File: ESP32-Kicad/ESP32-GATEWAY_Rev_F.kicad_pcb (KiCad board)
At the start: 2 copper layers, 50.8 x 62.2 mm, 66 parts, among them J1 Conn_01x07_Male, T1 DTC114YKA, U1 ACPL-217-56AE, U2 TLV62569DBVT(SOT23-5), U3 ESP32-WROOM-32D-4MB, U4 LAN8710A-EZC(QFN32), U5 ACPL-217-56AE

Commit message: Placa de kicad actualizada
Se agregaron los optoacopladores en los sensores de puerta, y se movieron los logos en la silkscreen de Ericnet y JLCPCB para la capa de atrás.
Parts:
- added G2: LOGO JLCPCB, Logos personales:jlcpcb_logo, B.Cu at (108.7, 114.6)
- added G3: LOGO ERICNET, Logos personales:ericnet_logo, B.Cu at (82.9, 114.8)
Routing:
- net GND: vias 173 -> 172

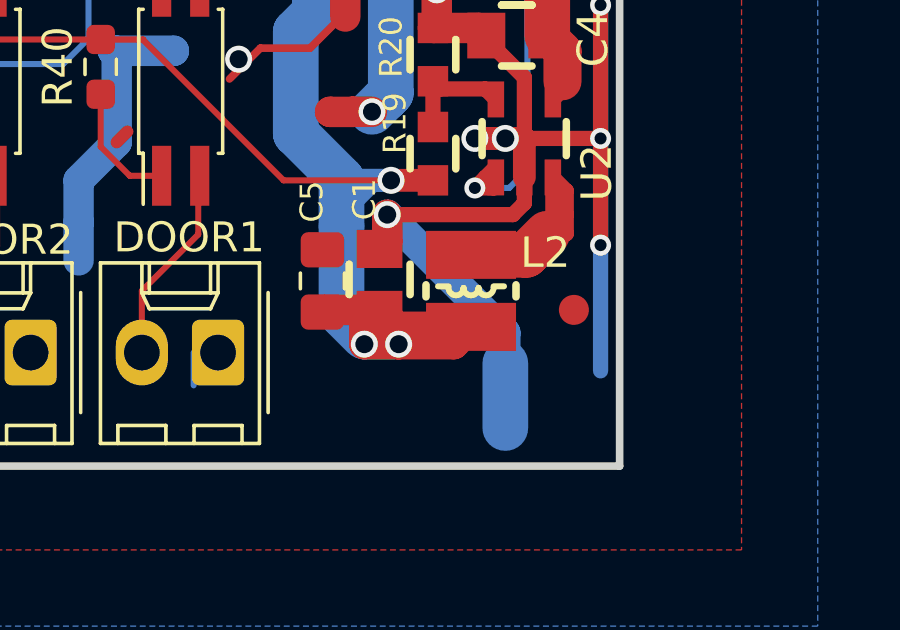
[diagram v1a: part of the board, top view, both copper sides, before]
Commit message: Proyecto en kicad actualizado
Se modificó el footprint del Inductor de la fuente
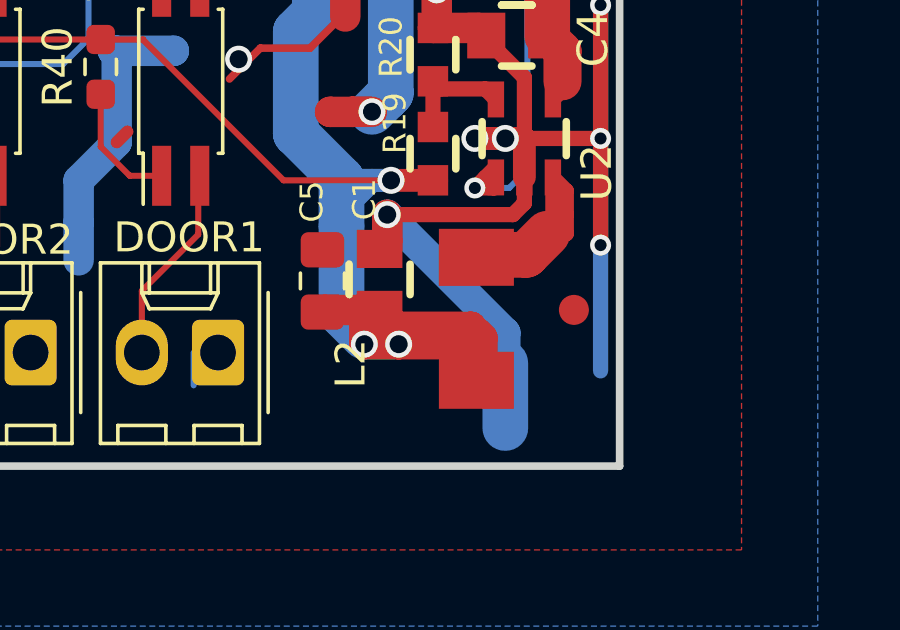
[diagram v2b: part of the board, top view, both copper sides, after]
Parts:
- L2: value 2.2uH/1.5A/DCR=35mR/20%/3.00x3.00x1.50mm/CD32(NR3015T2R2M) -> 2.2uH/9A/DCR=35mR/20%/3.00x3.00x1.50mm/CD32(NR3015T2R2M); footprint OLIMEX_RLC-FP:CD32 -> footprints_personales:SMD_0530
- moved L2 1.13 mm to (115.6, 122.3)
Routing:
- net +3V3: track 195.6 -> 197.8 mm

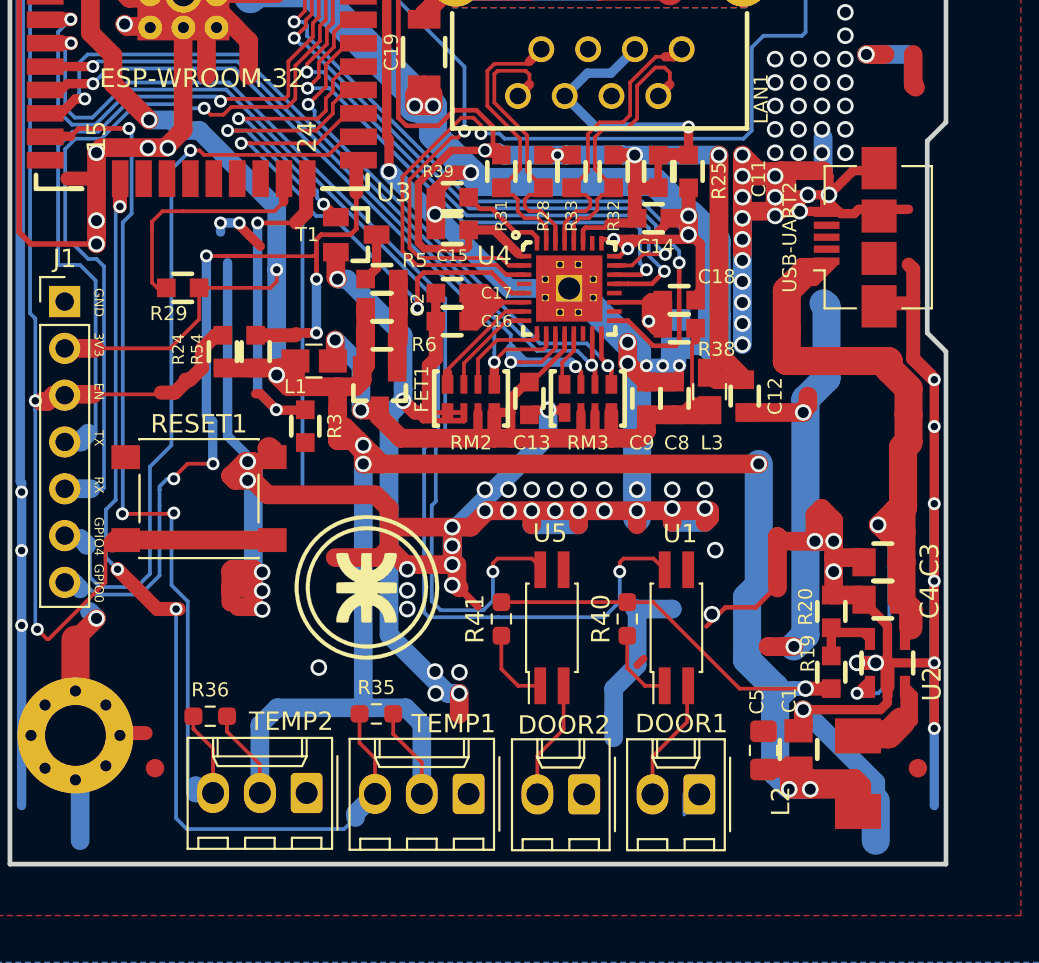
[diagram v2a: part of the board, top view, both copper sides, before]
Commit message: Se agregaron 2 sensores de puerta y se sacó uno de temperatura
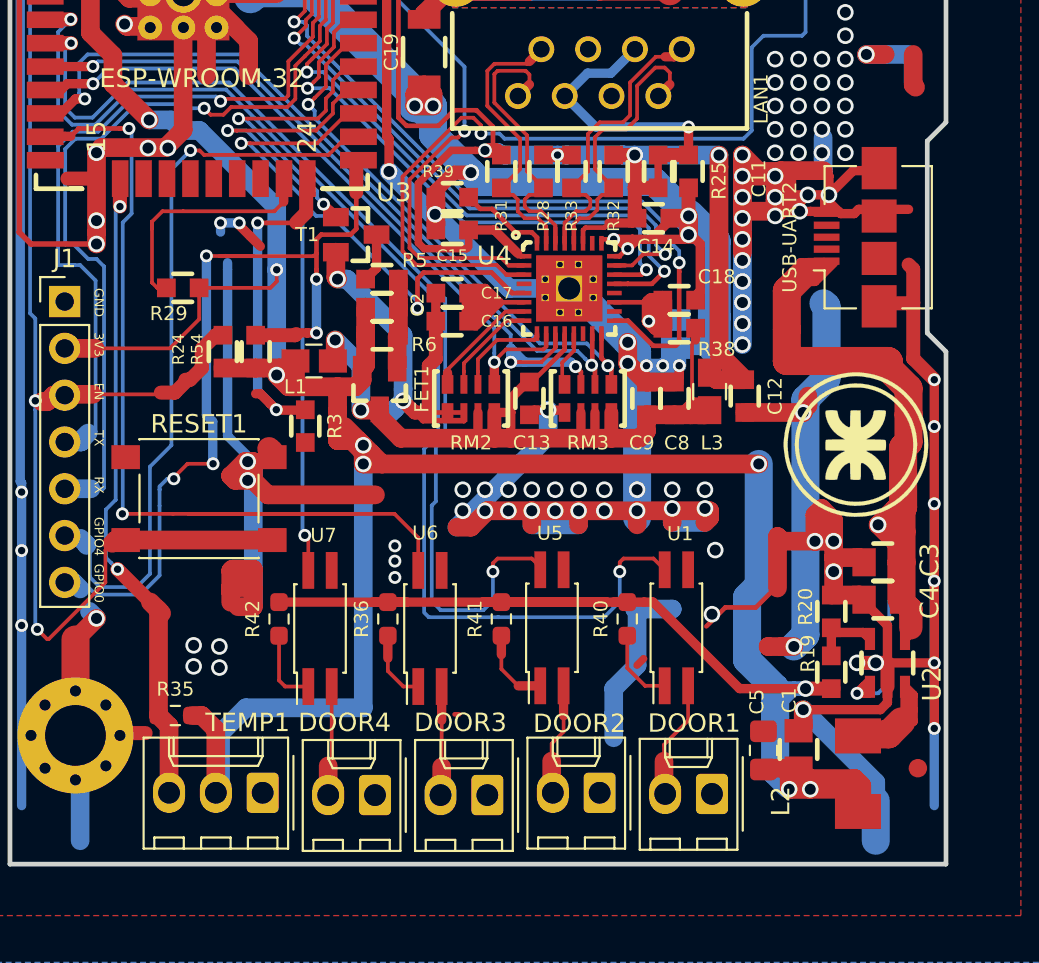
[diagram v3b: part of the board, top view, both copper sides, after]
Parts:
- removed FID1: Fiducial, OLIMEX_Other-FP:Fiducial1x3
- removed G1: Logo UTN, Logos personales:utn_logo
- removed TEMP2: Conn_01x03, Connector_Molex:Molex_KK-254_AE-6410-03A_1x03_P2.54mm_Vertical
- added DOOR3: Conn_01x02, Connector_Molex:Molex_KK-254_AE-6410-02A_1x02_P2.54mm_Vertical, F.Cu at (95.5, 125.5)
- added DOOR4: Conn_01x02, Connector_Molex:Molex_KK-254_AE-6410-02A_1x02_P2.54mm_Vertical, F.Cu at (89.4, 125.5)
- added G***: LOGO, Logos personales:utn_logo, F.Cu at (115.4, 106.6)
- added R42: 440/R0603, Resistor_SMD:R_0603_1608Metric_Pad0.98x0.95mm_HandSolder, F.Cu at (84.2, 116.0)
- added U6: ACPL-217-56AE, Package_SO:SO-4_4.4x2.3mm_P1.27mm, F.Cu at (92.4, 116.5)
- added U7: ACPL-217-56AE, Package_SO:SO-4_4.4x2.3mm_P1.27mm, F.Cu at (86.4, 116.5)
- R36: value 4.7K/R0603 -> 440/R0603
- moved TEMP1 11.2 mm to (83.3, 125.4)
- moved R36 11.0 mm to (90.1, 116.0), turned to 90 degrees
- moved R35 10.9 mm to (78.6, 121.2)
- moved DOOR2 0.84 mm to (101.6, 125.4)
- moved DOOR1 0.69 mm to (107.7, 125.5)
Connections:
- R36 pad 1: /GPIO14\TEMP2 -> Net-(R36-Pad1)
- U3 pad 13: /GPIO14\TEMP2 -> /GPIO14\DOOR3
- U3 pad 27: /GPIO16 -> /GPIO16\DOOR4
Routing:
- net /GPIO14\DOOR3: track 0.00 -> 54.0 mm, vias 0 -> 2
- net /GPIO14\TEMP2: track 51.1 -> 0.00 mm, vias 3 -> 0
- net GND: track 713.7 -> 672.1 mm, vias 172 -> 166
- net +3V3: track 197.8 -> 232.8 mm
- net /GPIO16\DOOR4: track 0.00 -> 32.1 mm, vias 0 -> 2
- net /GPIO16: track 27.8 -> 0.00 mm, vias 1 -> 0
- net /GPIO13\TEMP1: track 55.6 -> 35.9 mm, vias 3 -> 2
- net Net-(DOOR4-Pad2): track 0.00 -> 5.97 mm
- net Net-(DOOR3-Pad2): track 0.00 -> 5.92 mm
- net Net-(R36-Pad1): track 0.00 -> 4.69 mm
- net Net-(R42-Pad1): track 0.00 -> 3.92 mm
- net Net-(DOOR1-Pad2): track 6.69 -> 8.28 mm
- net Net-(DOOR2-Pad2): track 6.48 -> 7.81 mm

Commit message: Gerbers + ESP32 https server
Se agregaron gerbers y cambios finales de la placa. Se agrego un servidor https al codigo para el esp32
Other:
- board text added: "SNMP Hub Casas Daiana Pregelj Jose Riveros Rubén Vieiro Alexis"
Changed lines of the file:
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@@
   (general
     (thickness 1.6)
-    (drawings 19)
+    (drawings 20)
     (tracks 1715)
     (zones 0)
@@
   )
   (layers
-    (0 F.Cu mixed)
+    (0 F.Cu mixed hide)
     (31 B.Cu mixed)
     (32 B.Adhes user hide)
@@
     (35 F.Paste user hide)
     (36 B.SilkS user)
-    (37 F.SilkS user)
+    (37 F.SilkS user hide)
     (38 B.Mask user hide)
     (39 F.Mask user hide)
@@
     (42 Eco1.User user hide)
     (43 Eco2.User user hide)
-    (44 Edge.Cuts user hide)
+    (44 Edge.Cuts user)
     (45 Margin user hide)
     (46 B.CrtYd user hide)
@@
     (visible_elements 7FFDFF7F)
     (pcbplotparams
-      (layerselection 0x010fc_ffffffff)
+      (layerselection 0x3ffff_ffffffff)
       (usegerberextensions false)
       (usegerberattributes false)
@@
       (drillshape 0)
       (scaleselection 1)
-      (outputdirectory "../../../../Desktop/"))
+      (outputdirectory "Gerbers Propios/"))
   )
   (net 0 "")
@@
     (pad 2 thru_hole oval (at 2.54 0 180) (size 1.74 2.19) (drill 1.19) (layers *.Cu *.Mask)
       (net 74 "Net-(DOOR4-Pad2)"))
-    (pad 1 thru_hole roundrect (at 0 0 180) (size 1.74 2.19) (drill 1.19) (layers *.Cu *.Mask) (roundrect_rratio 0.143678)
+    (pad 1 thru_hole roundrect (at 0 0 180) (size 1.74 2.19) (drill 1.19) (layers *.Cu *.Mask) (roundrect_rratio 0.1436775862068966)
       (net 2 GND))
     (model ${KISYS3DMOD}/Connector_Molex.3dshapes/Molex_KK-254_AE-6410-02A_1x02_P2.54mm_Vertical.wrl
@@
     (pad 2 thru_hole oval (at 2.54 0 180) (size 1.74 2.19) (drill 1.19) (layers *.Cu *.Mask)
       (net 72 "Net-(DOOR3-Pad2)"))
-    (pad 1 thru_hole roundrect (at 0 0 180) (size 1.74 2.19) (drill 1.19) (layers *.Cu *.Mask) (roundrect_rratio 0.143678)
+    (pad 1 thru_hole roundrect (at 0 0 180) (size 1.74 2.19) (drill 1.19) (layers *.Cu *.Mask) (roundrect_rratio 0.1436775862068966)
       (net 2 GND))
     (model ${KISYS3DMOD}/Connector_Molex.3dshapes/Molex_KK-254_AE-6410-02A_1x02_P2.54mm_Vertical.wrl
@@
       (effects (font (size 0.5 0.5) (thickness 0.08)))
     )
-    (pad 2 smd roundrect (at 1.0375 0 90) (size 1.175 1.45) (layers F.Cu F.Paste F.Mask) (roundrect_rratio 0.212766)
+    (pad 2 smd roundrect (at 1.0375 0 90) (size 1.175 1.45) (layers F.Cu F.Paste F.Mask) (roundrect_rratio 0.2127659574468085)
       (net 2 GND))
-    (pad 1 smd roundrect (at -1.0375 0 90) (size 1.175 1.45) (layers F.Cu F.Paste F.Mask) (roundrect_rratio 0.212766)
+    (pad 1 smd roundrect (at -1.0375 0 90) (size 1.175 1.45) (layers F.Cu F.Paste F.Mask) (roundrect_rratio 0.2127659574468085)
       (net 3 +3V3))
     (model ${KISYS3DMOD}/Capacitor_SMD.3dshapes/C_0805_2012Metric.wrl
@@
     (pad 2 thru_hole oval (at 2.54 0 180) (size 1.74 2.19) (drill 1.19) (layers *.Cu *.Mask)
       (net 3 +3V3))
-    (pad 1 thru_hole roundrect (at 0 0 180) (size 1.74 2.19) (drill 1.19) (layers *.Cu *.Mask) (roundrect_rratio 0.143678)
+    (pad 1 thru_hole roundrect (at 0 0 180) (size 1.74 2.19) (drill 1.19) (layers *.Cu *.Mask) (roundrect_rratio 0.1436775862068966)
       (net 2 GND))
     (model ${KISYS3DMOD}/Connector_Molex.3dshapes/Molex_KK-254_AE-6410-03A_1x03_P2.54mm_Vertical.wrl
@@
     (pad 2 thru_hole oval (at 2.54 0 180) (size 1.74 2.19) (drill 1.19) (layers *.Cu *.Mask)
       (net 69 "Net-(DOOR2-Pad2)"))
-    (pad 1 thru_hole roundrect (at 0 0 180) (size 1.74 2.19) (drill 1.19) (layers *.Cu *.Mask) (roundrect_rratio 0.143678)
+    (pad 1 thru_hole roundrect (at 0 0 180) (size 1.74 2.19) (drill 1.19) (layers *.Cu *.Mask) (roundrect_rratio 0.1436775862068966)
       (net 2 GND))
     (model ${KISYS3DMOD}/Connector_Molex.3dshapes/Molex_KK-254_AE-6410-02A_1x02_P2.54mm_Vertical.wrl
@@
     (pad 2 thru_hole oval (at 2.54 0 180) (size 1.74 2.19) (drill 1.19) (layers *.Cu *.Mask)
       (net 68 "Net-(DOOR1-Pad2)"))
-    (pad 1 thru_hole roundrect (at 0 0 180) (size 1.74 2.19) (drill 1.19) (layers *.Cu *.Mask) (roundrect_rratio 0.143678)
+    (pad 1 thru_hole roundrect (at 0 0 180) (size 1.74 2.19) (drill 1.19) (layers *.Cu *.Mask) (roundrect_rratio 0.1436775862068966)
       (net 2 GND))
     (model ${KISYS3DMOD}/Connector_Molex.3dshapes/Molex_KK-254_AE-6410-02A_1x02_P2.54mm_Vertical.wrl
@@
     )
   )
+  (gr_text "SNMP Hub\nCasas Daiana\nPregelj Jose\nRiveros Rubén\nVieiro Alexis" (at 95.758 120.269) (layer B.SilkS)
+    (effects (font (size 1 1) (thickness 0.15)) (justify mirror))
+  )
   (gr_text GPIO0 (at 74.422 114.046 270) (layer F.SilkS)
